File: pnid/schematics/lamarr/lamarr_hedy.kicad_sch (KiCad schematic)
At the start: 93 parts

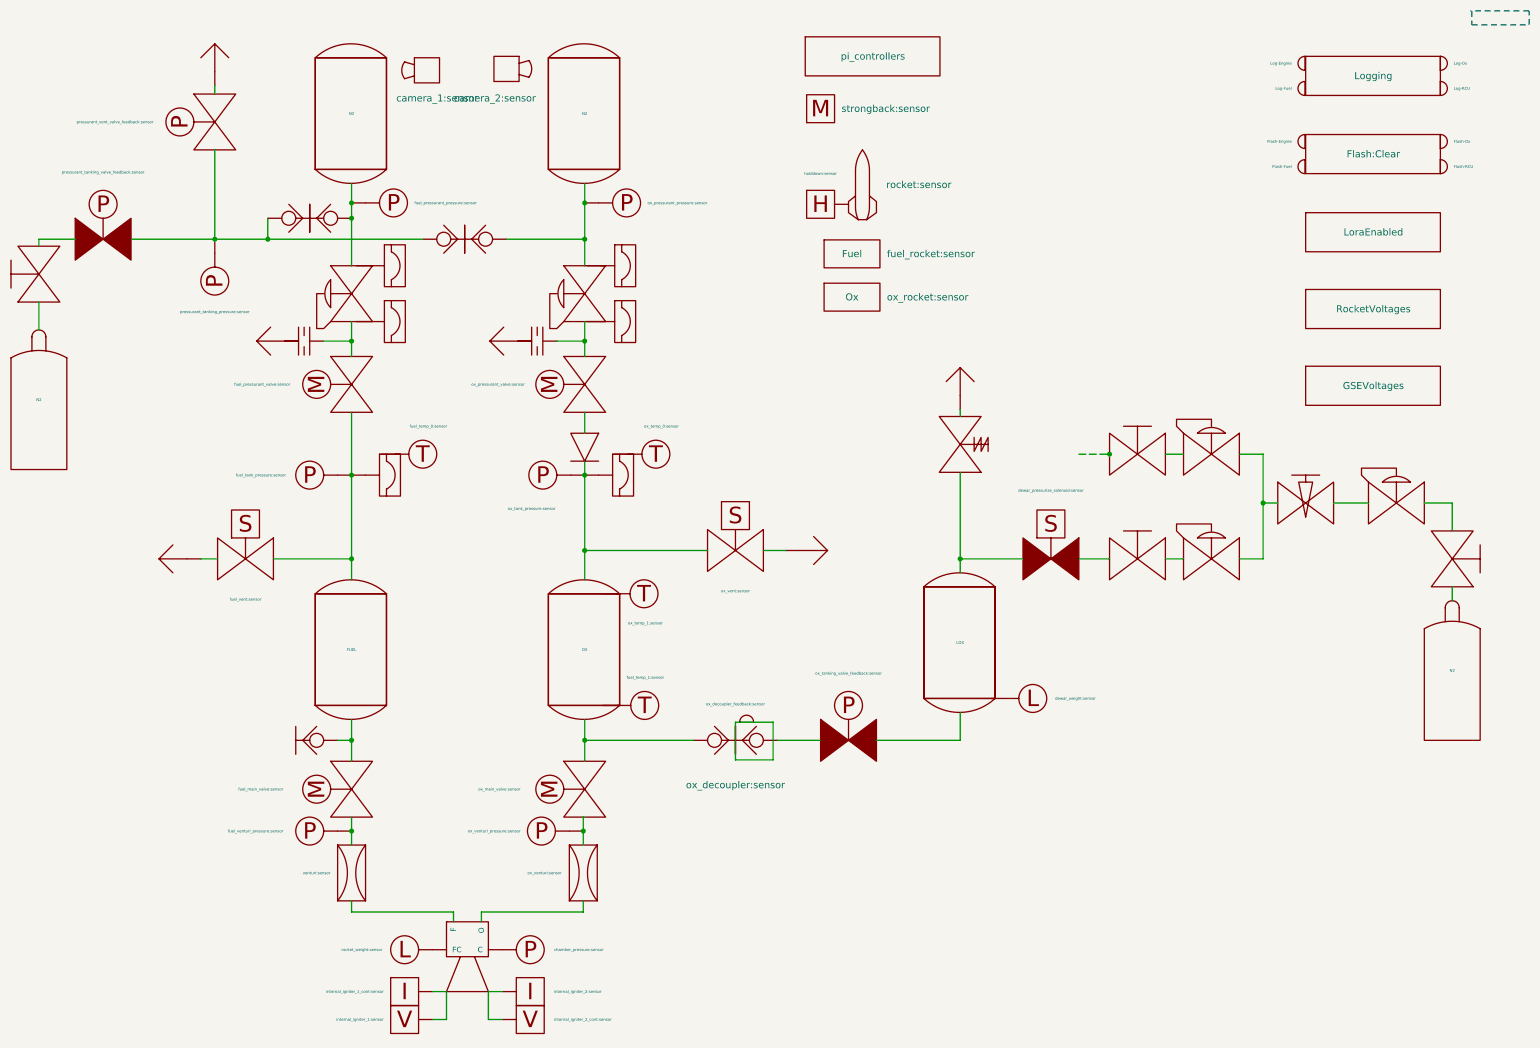
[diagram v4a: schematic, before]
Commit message: Added Temp Sensors (Location TBA)
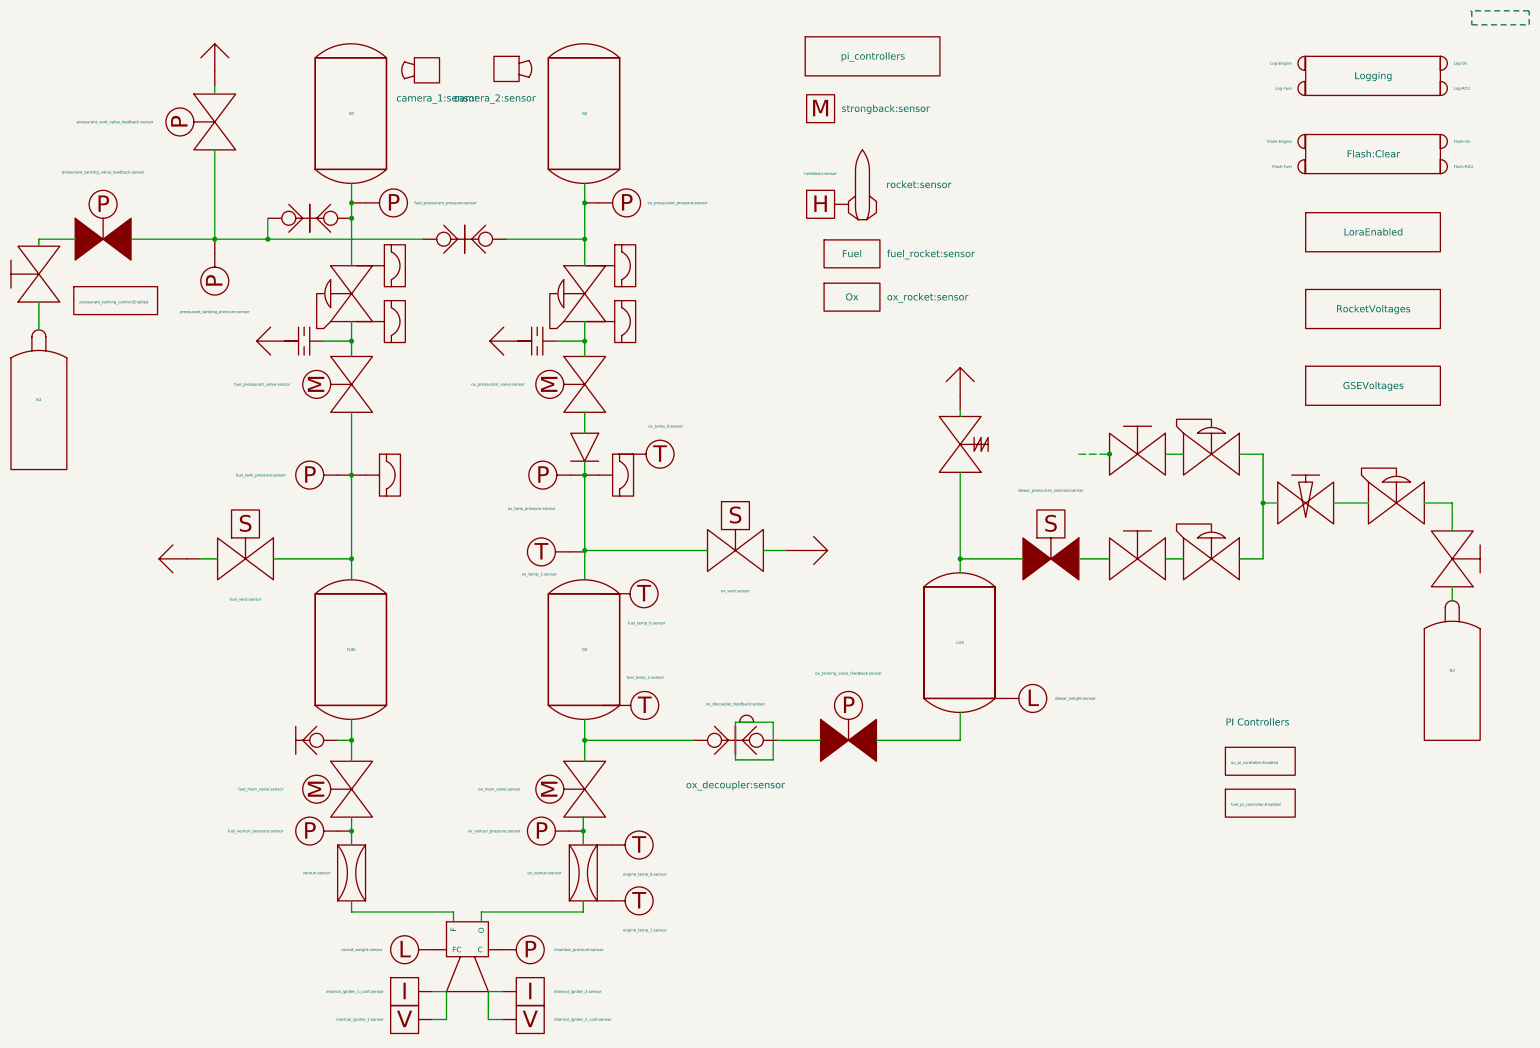
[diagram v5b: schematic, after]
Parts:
- removed fuel_manifold_temperature: fuel_temp_0:sensor, symbol PnID-Lib:Sensor_Temperature
- added fuel_pi_controller: fuel_pi_controller:Enabled, symbol PnID:Label
- added ox_main_valve_temperature: engine_temp_0:sensor, symbol PnID-Lib:Sensor_Temperature
- added ox_main_valve_temperature_1: engine_temp_1:sensor, symbol PnID-Lib:Sensor_Temperature
- added ox_mainfold_temperature_1: ox_temp_1:sensor, symbol PnID-Lib:Sensor_Temperature
- added ox_pi_controller: ox_pi_controller:Enabled, symbol PnID:Label
- added pressure_control: pressurant_tanking_control:Enabled, symbol PnID:Label
- ox_tank_top_temperature: value ox_temp_1:sensor -> fuel_temp_0:sensor
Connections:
- net at engine.~ (O): now also venturi1.~; no longer ox_venturi.~
- net at venturi1.~: now also fuel_main_valve.~, fuel_venturi_pressure.~; no longer engine.~ (O)
- net at dewar_needle_valve?.~: now also C2.~, C3.~; no longer C1.~
- net at Orifice2.~: now also fuel_pressurant_valve.~, pressurantPressureRegulator1.~
- new net: engine.~ (O), ox_venturi.~
- new net: OX.~, ox_main_valve.~, ox_quick_connect.~
- new net: DewarOverPressureValve?.~, LOX.~, dewar_pressurize_solenoid.~
- new net: C1.~, dewar_needle_valve?.~
- new net: Orifice1.~, ox_pressurant_valve.~, pressurantPressureRegulator2.~
- new net: FUEL.~, fuel_main_valve.~, ox_quick_connect1.~
- now unconnected: Orifice1.~
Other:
- note added: "PI Controllers"

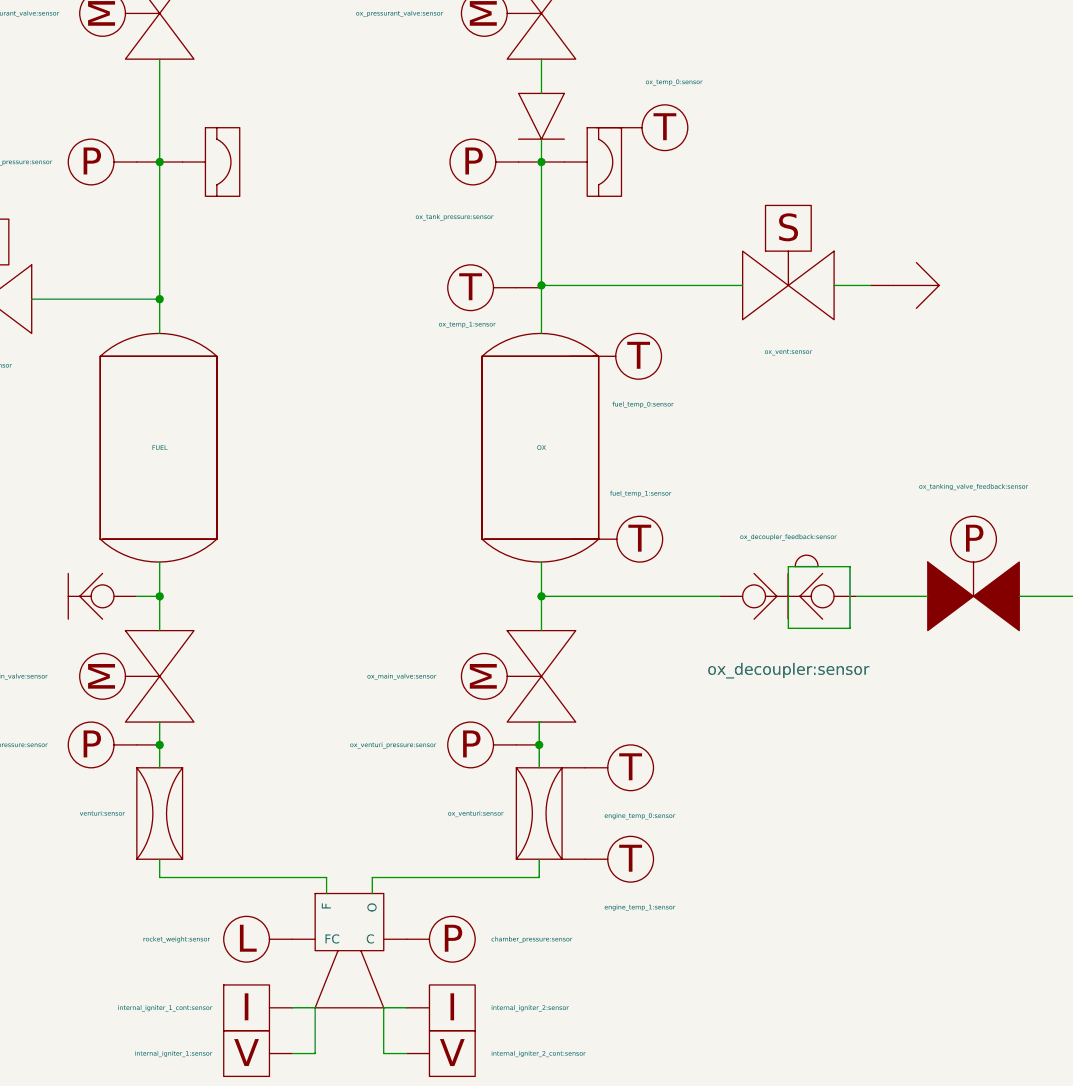
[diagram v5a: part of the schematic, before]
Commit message: Update lamarr_hedy.kicad_sch
Changed Temperature Channel locations
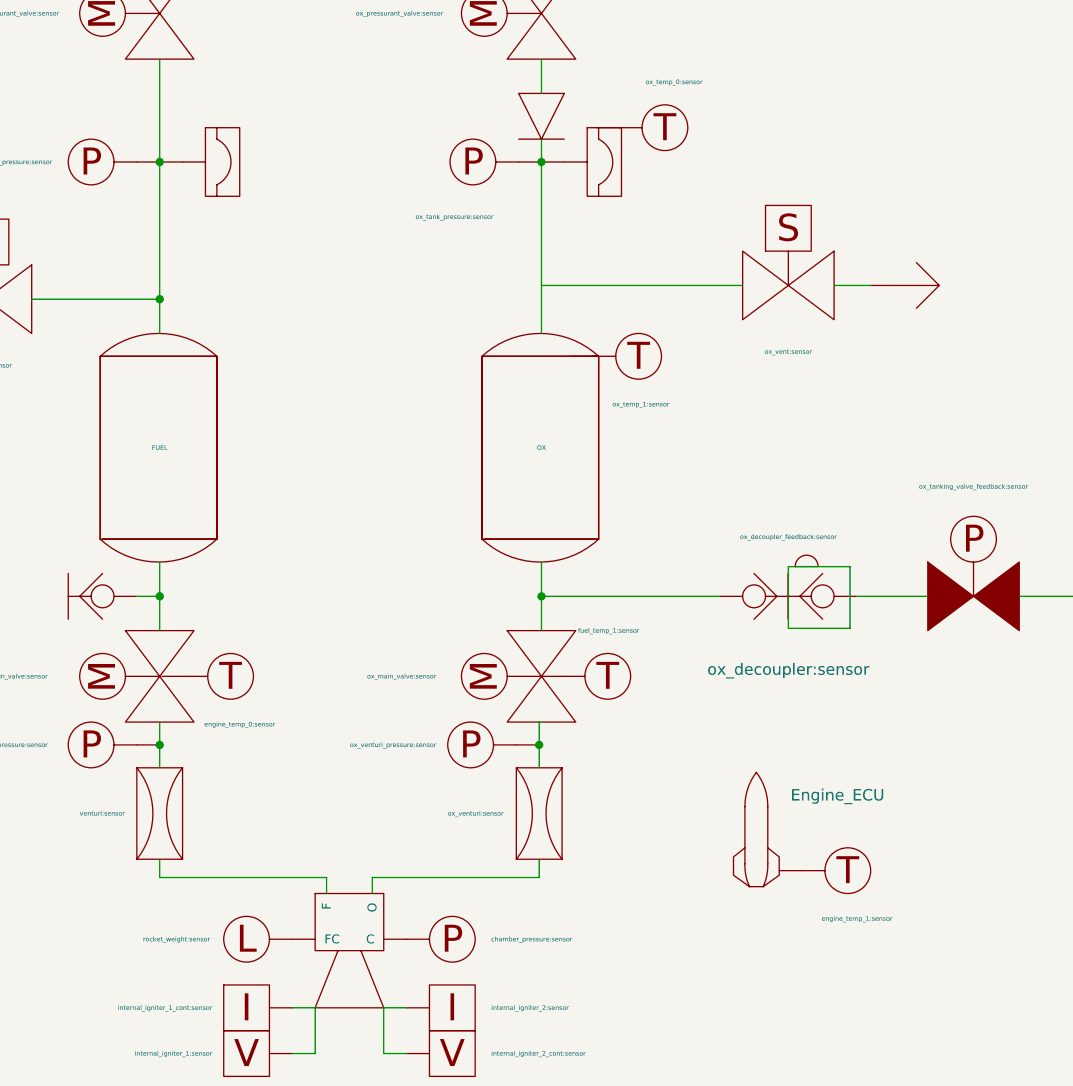
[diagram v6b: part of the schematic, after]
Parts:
- removed ox_mainfold_temperature_1: ox_temp_1:sensor, symbol PnID-Lib:Sensor_Temperature
- added Engine_ECU: (no value), symbol PnID:Rocket_Channel
- ox_tank_top_temperature: value fuel_temp_0:sensor -> ox_temp_1:sensor
- renumbered ox_manifold_temperature to burst_disk_temperature, ox_main_valve_temperature_1 to engine_ECU_temperature, ox_main_valve_temperature to fuel_main_valve_temperature, ox_tank_bottom_temperature to ox_main_valve_servo_temperature
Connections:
- net at engine.~ (O): now also venturi1.~; no longer ox_venturi.~
- net at venturi1.~: now also fuel_main_valve.~, fuel_venturi_pressure.~; no longer engine.~ (O)
- net at dewar_needle_valve?.~: now also C2.~, C3.~; no longer C1.~
- net at BurstDisc1.~, CheckValve2.~, OX.~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: no longer ox_vent.~
- net at Orifice2.~: now also fuel_pressurant_valve.~, pressurantPressureRegulator1.~
- new net: engine.~ (O), ox_venturi.~
- new net: OX.~, ox_main_valve.~, ox_quick_connect.~
- new net: DewarOverPressureValve?.~, LOX.~, dewar_pressurize_solenoid.~
- new net: C1.~, dewar_needle_valve?.~
- new net: Orifice1.~, ox_pressurant_valve.~, pressurantPressureRegulator2.~
- new net: FUEL.~, fuel_main_valve.~, ox_quick_connect1.~
- now unconnected: Orifice1.~
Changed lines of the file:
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@@
 	)
 	(junction
-		(at 120.904 112.776)
-		(diameter 0)
-		(color 0 0 0 0)
-	)
-	(junction
 		(at 78.486 147.32)
 		(diameter 0)
@@
 	(wire
 		(pts
-			(xy 120.904 99.06) (xy 120.904 112.776)
-		)
-		(stroke
-			(width 0)
-			(type default)
-		)
-	)
-	(wire
-		(pts
 			(xy 75.946 147.32) (xy 78.486 147.32)
 		)
@@
 	(wire
 		(pts
-			(xy 120.904 112.776) (xy 120.904 118.11)
+			(xy 120.904 99.06) (xy 120.904 118.11)
 		)
 		(stroke
@@
 	)
 	(symbol
+		(lib_id "PnID:Rocket_Channel")
+		(at 144.78 175.26 0)
+		(unit 1)
+		(exclude_from_sim no)
+		(in_bom yes)
+		(on_board yes)
+		(dnp no)
+		(fields_autoplaced yes)
+		(property "Reference" "Engine_ECU"
+			(at 148.59 169.4179 0)
+			(effects
+				(font
+					(size 1.27 1.27)
+				)
+				(justify left)
+			)
+		)
+		(property "Value" ""
+			(at 148.59 170.6879 0)
+			(effects
+				(font
+					(size 1.27 1.27)
+				)
+				(justify left)
+			)
+		)
+		(property "Footprint" ""
+			(at 144.78 178.308 0)
+			(effects
+				(font
+					(size 1.27 1.27)
+				)
+				(hide yes)
+			)
+		)
+		(property "Datasheet" ""
+			(at 144.78 178.308 0)
+			(effects
+				(font
+					(size 1.27 1.27)
+				)
+				(hide yes)
+			)
+		)
+		(property "Description" ""
+			(at 144.78 175.26 0)
+			(effects
+				(font
+					(size 1.27 1.27)
+				)
+				(hide yes)
+			)
+		)
+		(property "Unit" " "
+			(at 148.59 171.9579 0)
+			(effects
+				(font
+					(size 1.27 1.27)
+				)
+				(justify left)
+			)
+		)
+		(property "Action_Reference" " "
+			(at 148.59 174.4979 0)
+			(effects
+				(font
+					(size 1.27 1.27)
+				)
+				(justify left)
+			)
+		)
+		(property "Data_Content" " "
+			(at 148.59 177.0379 0)
+			(effects
+				(font
+					(size 1.27 1.27)
+				)
+				(justify left)
+			)
+		)
+		(instances
+			(project ""
+				(path "/604fc9f3-63a6-4133-afd1-4a5c2507dc1d"
+					(reference "Engine_ECU")
+					(unit 1)
+				)
+			)
+		)
+	)
+	(symbol
 		(lib_id "PnID-Lib:PressureRegulator")
 		(at 120.904 66.04 90)
@@
 		(on_board yes)
 		(dnp no)
-		(property "Reference" "ox_manifold_temperature"
+		(property "Reference" "burst_disk_temperature"
 			(at 138.43 94.615 0)
 			(effects
@@
 			(project "lamarr_hedy"
 				(path "/604fc9f3-63a6-4133-afd1-4a5c2507dc1d"
-					(reference "ox_manifold_temperature")
+					(reference "burst_disk_temperature")
 					(unit 1)
 				)
@@
 			)
 		)
-		(property "Value" "fuel_temp_0:sensor"
+		(property "Value" "ox_temp_1:sensor"
 			(at 128.778 125.984 0)
 			(effects
@@
 	)
 	(symbol
-		(lib_name "Sensor_Temperature_1")
-		(lib_id "PnID-Lib:Sensor_Temperature")
-		(at 115.57 113.03 0)
-		(unit 1)
-		(exclude_from_sim no)
-		(in_bom yes)
-		(on_board yes)
-		(dnp no)
-		(property "Reference" "ox_mainfold_temperature_1"
-			(at 107.696 109.22 0)
-			(effects
-				(font
-					(size 0.508 0.508)
-				)
-				(justify left)
-				(hide yes)
-			)
-		)
-		(property "Value" "ox_temp_1:sensor"
-			(at 109.474 117.094 0)
-			(effects
-				(font
-					(size 0.508 0.508)
-				)
-				(justify left)
-			)
-		)
-		(property "Footprint" ""
-			(at 113.03 113.03 0)
-			(effects
-				(font
-					(size 0.508 0.508)
-				)
-				(hide yes)
-			)
-		)
-		(property "Datasheet" ""
-			(at 113.03 113.03 0)
-			(effects
-				(font
-					(size 0.508 0.508)
-				)
-				(hide yes)
-			)
-		)
-		(property "Description" ""
-			(at 113.03 113.03 0)
-			(effects
-				(font
-					(size 1.27 1.27)
-				)
-				(hide yes)
-			)
-		)
-		(property "Unit" "˚C"
-			(at 113.03 113.03 0)
-			(effects
-				(font
-					(size 0.508 0.508)
-				)
-				(hide yes)
-			)
-		)
-		(property "Action_Reference" " "
-			(at 113.03 113.03 0)
-			(effects
-				(font
-					(size 1.27 1.27)
-				)
-				(hide yes)
-			)
-		)
-		(pin "~"
-		)
-		(instances
-			(project "lamarr_hedy"
-				(path "/604fc9f3-63a6-4133-afd1-4a5c2507dc1d"
-					(reference "ox_mainfold_temperature_1")
-					(unit 1)
-				)
-			)
-		)
-	)
-	(symbol
 		(lib_id "PnID-Lib:Label")
 		(at 264.414 40.64 0)
@@
 	(symbol
 		(lib_id "PnID-Lib:Sensor_Temperature")
-		(at 131.826 140.97 0)
+		(at 128.27 156.21 0)
 		(unit 1)
 		(exclude_from_sim no)
@@
 		(on_board yes)
 		(dnp no)
-		(property "Reference" "ox_tank_bottom_temperature"
-			(at 135.636 140.335 0)
+		(property "Reference" "ox_main_valve_servo_temperature"
+			(at 132.08 155.575 0)
 			(effects
 				(font
@@
 		)
 		(property "Value" "fuel_temp_1:sensor"
-			(at 128.524 135.89 0)
+			(at 124.968 151.13 0)
 			(effects
 				(font
@@
 		)
 		(property "Footprint" ""
-			(at 131.826 140.97 0)
+			(at 128.27 156.21 0)
 			(effects
 				(font
@@
 		)
 		(property "Datasheet" ""
-			(at 131.826 140.97 0)
+			(at 128.27 156.21 0)
 			(effects
 				(font
@@
 		)
 		(property "Description" ""
-			(at 131.826 140.97 0)
+			(at 128.27 156.21 0)
 			(effects
 				(font
@@
 		)
 		(property "Unit" "˚C"
-			(at 131.826 140.97 0)
+			(at 128.27 156.21 0)
 			(effects
 				(font
@@
 		)
 		(property "Action_Reference" " "
-			(at 131.826 140.97 0)
+			(at 128.27 156.21 0)
 			(effects
 				(font
@@
 			(project ""
 				(path "/604fc9f3-63a6-4133-afd1-4a5c2507dc1d"
-					(reference "ox_tank_bottom_temperature")
+					(reference "ox_main_valve_servo_temperature")
 					(unit 1)
 				)
@@
 	(symbol
 		(lib_id "PnID-Lib:Sensor_Temperature")
-		(at 130.81 176.53 0)
+		(at 154.94 177.8 0)
 		(unit 1)
 		(exclude_from_sim no)
@@
 		(on_board yes)
 		(dnp no)
-		(property "Reference" "ox_main_valve_temperature_1"
-			(at 134.62 175.895 0)
+		(property "Reference" "engine_ECU_temperature"
+			(at 158.75 177.165 0)
 			(effects
 				(font
@@
 		)
 		(property "Value" "engine_temp_1:sensor"
-			(at 127.889 181.864 0)
+			(at 152.019 183.134 0)
 			(effects
 				(font
@@
 		)
 		(property "Footprint" ""
-			(at 130.81 176.53 0)
+			(at 154.94 177.8 0)
 			(effects
 				(font
@@
 		)
 		(property "Datasheet" ""
-			(at 130.81 176.53 0)
+			(at 154.94 177.8 0)
 			(effects
 				(font
@@
 		)
 		(property "Description" ""
-			(at 130.81 176.53 0)
+			(at 154.94 177.8 0)
 			(effects
 				(font
@@
 		)
 		(property "Unit" "˚C"
-			(at 130.81 176.53 0)
+			(at 154.94 177.8 0)
 			(effects
 				(font
@@
 		)
 		(property "Action_Reference" " "
-			(at 130.81 176.53 0)
+			(at 154.94 177.8 0)
 			(effects
 				(font
@@
 			(project "lamarr_hedy"
 				(path "/604fc9f3-63a6-4133-afd1-4a5c2507dc1d"
-					(reference "ox_main_valve_temperature_1")
+					(reference "engine_ECU_temperature")
 					(unit 1)
 				)
@@
 	(symbol
 		(lib_id "PnID-Lib:Sensor_Temperature")
-		(at 130.81 166.37 0)
+		(at 86.36 156.21 0)
 		(unit 1)
 		(exclude_from_sim no)
@@
 		(on_board yes)
 		(dnp no)
-		(property "Reference" "ox_main_valve_temperature"
-			(at 134.62 165.735 0)
+		(property "Reference" "fuel_main_valve_temperature"
+			(at 90.17 155.575 0)
 			(effects
 				(font
@@
 		)
 		(property "Value" "engine_temp_0:sensor"
-			(at 127.889 171.704 0)
+			(at 83.439 161.544 0)
 			(effects
 				(font
@@
 		)
 		(property "Footprint" ""
-			(at 130.81 166.37 0)
+			(at 86.36 156.21 0)
 			(effects
 				(font
@@
 		)
 		(property "Datasheet" ""
-			(at 130.81 166.37 0)
+			(at 86.36 156.21 0)
 			(effects
 				(font
@@
 		)
 		(property "Description" ""
-			(at 130.81 166.37 0)
+			(at 86.36 156.21 0)
 			(effects
 				(font
@@
 		)
 		(property "Unit" "˚C"
-			(at 130.81 166.37 0)
+			(at 86.36 156.21 0)
 			(effects
 				(font
@@
 		)
 		(property "Action_Reference" " "
-			(at 130.81 166.37 0)
+			(at 86.36 156.21 0)
 			(effects
 				(font
@@
 			(project "lamarr_hedy"
 				(path "/604fc9f3-63a6-4133-afd1-4a5c2507dc1d"
-					(reference "ox_main_valve_temperature")
+					(reference "fuel_main_valve_temperature")
 					(unit 1)
 				)
